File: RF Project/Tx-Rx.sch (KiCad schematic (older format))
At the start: 25 parts, among them U1 CC2500RGPR, U2 U.FL_male

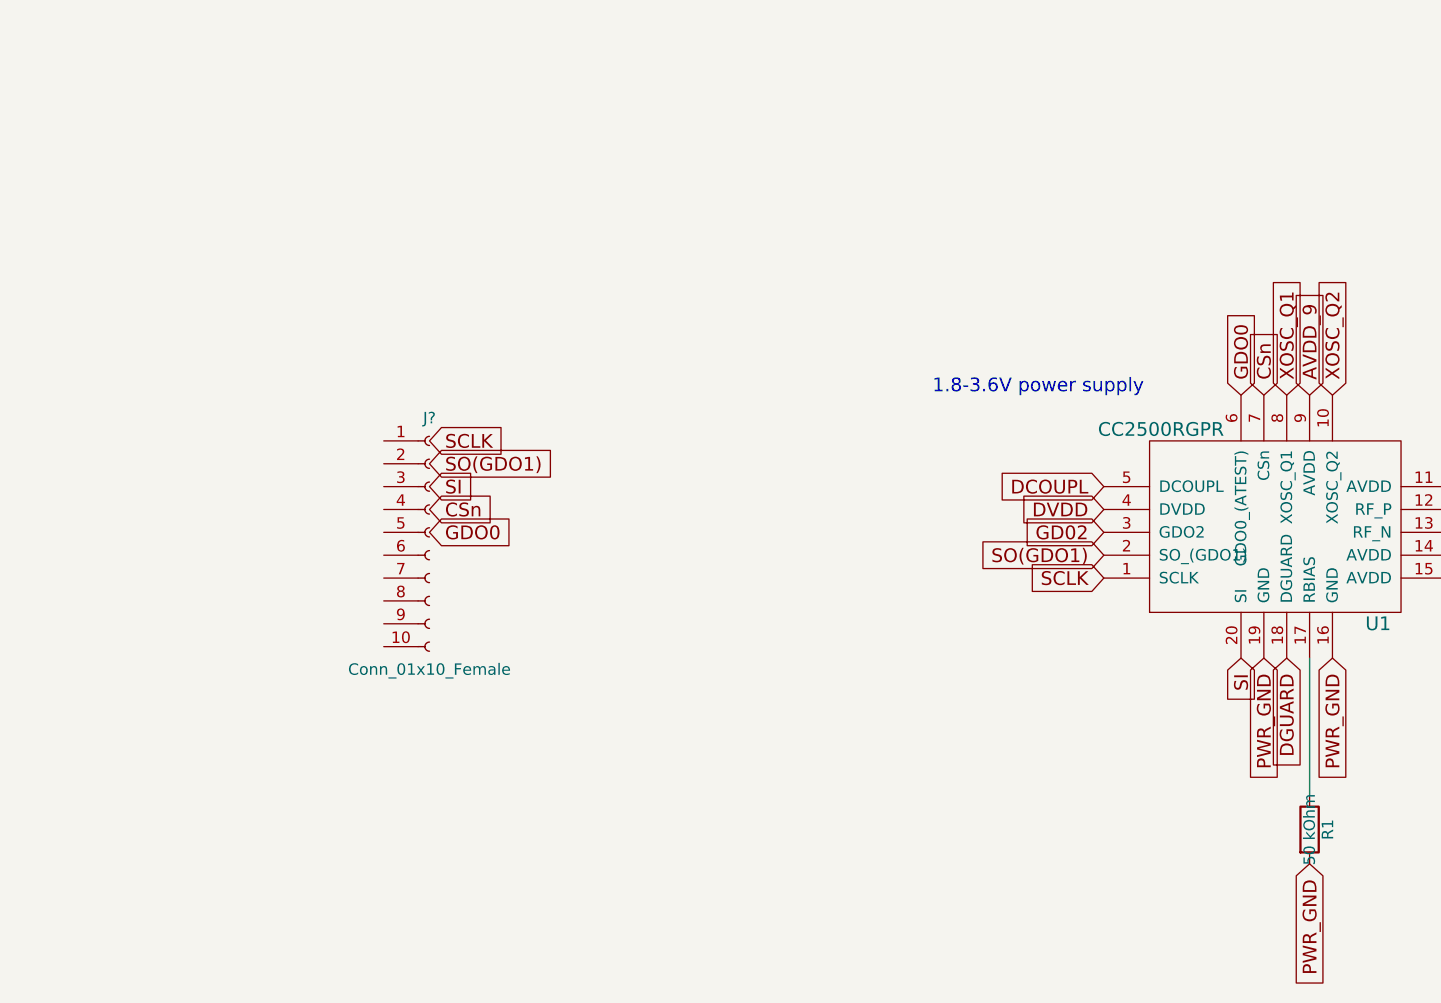
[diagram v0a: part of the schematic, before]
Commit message: Added Avionics Headers to schematic, fixed library link issues (hopefully) and started working on Layout
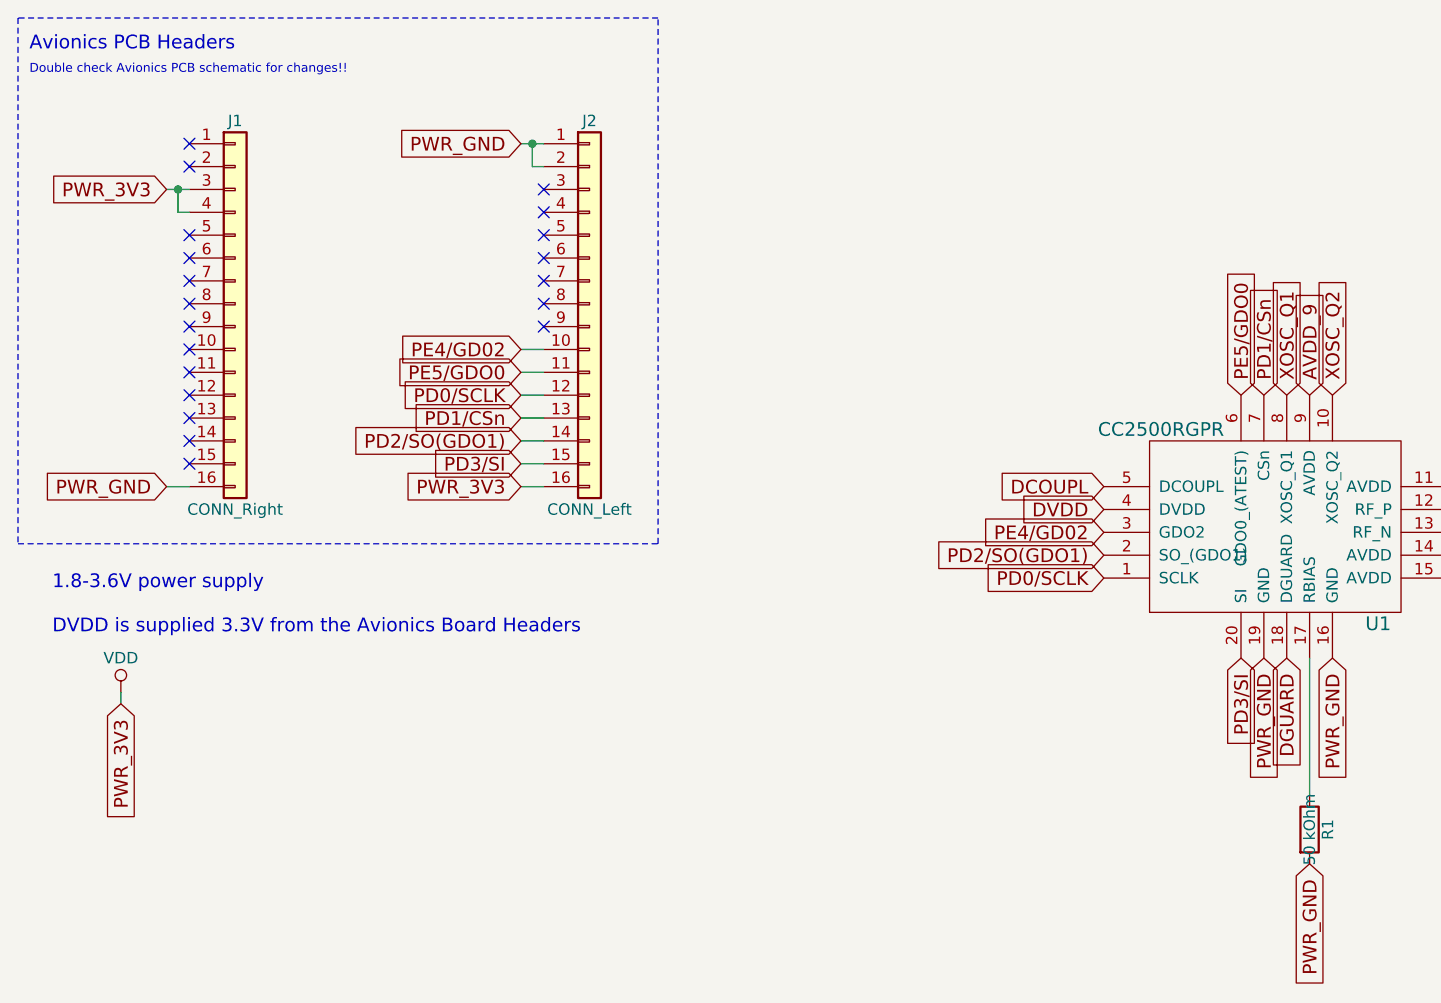
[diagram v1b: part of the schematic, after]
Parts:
- removed J?: Conn_01x10_Female, symbol Conn_01x10_Female
- added J1: CONN_Right, Pin_Headers:Pin_Header_Straight_1x16_Pitch2.54mm, symbol Conn_01x16
- added J2: CONN_Left, Pin_Headers:Pin_Header_Straight_1x16_Pitch2.54mm, symbol Conn_01x16
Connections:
- net GNDREF: now also J1.16 (Pin_16), J2.1 (Pin_1), J2.2 (Pin_2)
- net VDD: now also J1.3 (Pin_3), J1.4 (Pin_4), J2.16 (Pin_16)
- net CSn renamed PD1/CSn
- net PD1/CSn: now also J2.13 (Pin_13)
- net GD02 renamed PE4/GD02
- net PE4/GD02: now also J2.10 (Pin_10)
- net GDO0 renamed PE5/GDO0
- net PE5/GDO0: now also J2.11 (Pin_11)
- net SCLK renamed PD0/SCLK
- net PD0/SCLK: now also J2.12 (Pin_12)
- net SI renamed PD3/SI
- net PD3/SI: now also J2.15 (Pin_15)
- net SO(GDO1) renamed PD2/SO(GDO1)
- net PD2/SO(GDO1): now also J2.14 (Pin_14)
- no-connect marks 0 -> 20
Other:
- note added: "1.8-3.6V power supply\n\nDVDD is supplied 3.3V from the Avionics Board Headers\n"
- note added: "Avionics PCB Headers"
- note added: "Double check Avionics PCB schematic for changes!!"
- note removed: "1.8-3.6V power supply\n"

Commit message: Add files via upload
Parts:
- C14, C16, C17: value 220μF -> 220pF
- R1: footprint Resistors_SMD:R_0201 -> Resistors_SMD:R_0402
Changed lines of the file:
@@
 F 0 "R1" V 6330 4150 50  0000 C CNN
 F 1 "50 kOhm" V 6250 4150 50  0000 C CNN
-F 2 "Resistors_SMD:R_0201" V 6180 4150 50  0001 C CNN
+F 2 "Resistors_SMD:R_0402" V 6180 4150 50  0001 C CNN
 F 3 "" H 6250 4150 50  0001 C CNN
 	1    6250 4150
@@
 P 9550 1750
 F 0 "C14" H 9575 1850 50  0000 L CNN
-F 1 "220μF" H 9575 1650 50  0000 L CNN
+F 1 "220pF" H 9575 1650 50  0000 L CNN
 F 2 "Capacitors_SMD:C_0402" H 9588 1600 50  0001 C CNN
 F 3 "" H 9550 1750 50  0001 C CNN
@@
 P 10300 1750
 F 0 "C16" H 10325 1850 50  0000 L CNN
-F 1 "220μF" H 10325 1650 50  0000 L CNN
+F 1 "220pF" H 10325 1650 50  0000 L CNN
 F 2 "Capacitors_SMD:C_0402" H 10338 1600 50  0001 C CNN
 F 3 "" H 10300 1750 50  0001 C CNN
@@
 P 10550 2650
 F 0 "C17" H 10575 2750 50  0000 L CNN
-F 1 "220μF" H 10575 2550 50  0000 L CNN
+F 1 "220pF" H 10575 2550 50  0000 L CNN
 F 2 "Capacitors_SMD:C_0402" H 10588 2500 50  0001 C CNN
 F 3 "" H 10550 2650 50  0001 C CNN

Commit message: hello
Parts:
- R1: value 50 kOhm -> 56.2 kOhm; Digikey Part No. (none) -> CR0402-FX-5622GLFCT-ND
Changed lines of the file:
@@
 P 6250 4150
 F 0 "R1" V 6330 4150 50  0000 C CNN
-F 1 "50 kOhm" V 6250 4150 50  0000 C CNN
+F 1 "56.2 kOhm" V 6250 4150 50  0000 C CNN
 F 2 "Resistors_SMD:R_0402" V 6180 4150 50  0001 C CNN
 F 3 "" H 6250 4150 50  0001 C CNN
+F 4 "CR0402-FX-5622GLFCT-ND" V 6250 4150 60  0001 C CNN "Digikey Part No."
 	1    6250 4150
 	1    0    0    -1

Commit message: GPS schematic and pcb track routing
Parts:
- 26Mhtz1: footprint Crystals:Crystal_SMD_Abracon_ABM3B-4pin_5.0x3.2mm -> transciever_chip:CC2500
- C1: footprint Capacitors_SMD:C_0402 -> RF_Transciever:VENUS634FLPX
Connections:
- net RX: now reaches J1.8 (Pin_8)
- net TX: now reaches J1.9 (Pin_9)
- no-connect marks 20 -> 18
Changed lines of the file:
@@
 LIBS:cc2500rgpr
 LIBS:Tx-Rx-cache
+LIBS:rocketGPS
 EELAYER 25 0
 EELAYER END
 $Descr A4 11693 8268
 encoding utf-8
-Sheet 1 1
+Sheet 1 2
 Title "Model Rocket Transciever Design"
 Date "2018-07-13"
@@
 F 0 "26Mhtz1" H 8200 4250 50  0000 C CNN
 F 1 "Crystal" H 8200 3950 50  0000 C CNN
-F 2 "Crystals:Crystal_SMD_Abracon_ABM3B-4pin_5.0x3.2mm" H 8200 4100 50  0001 C CNN
+F 2 "transciever_chip:CC2500" H 8200 4100 50  0001 C CNN
 F 3 "" H 8200 4100 50  0001 C CNN
 	1    8200 4100
@@
 F 0 "C1" H 8125 5500 50  0000 L CNN
 F 1 "100pF" H 8125 5300 50  0000 L CNN
-F 2 "Capacitors_SMD:C_0402" H 8138 5250 50  0001 C CNN
+F 2 "RF_Transciever:VENUS634FLPX" H 8138 5250 50  0001 C CNN
 F 3 "" H 8100 5400 50  0001 C CNN
 	1    8100 5400
@@
 NoConn ~ 1350 1250
 NoConn ~ 1350 1550
-NoConn ~ 1350 1650
 NoConn ~ 1350 1750
-NoConn ~ 1350 1850
-NoConn ~ 1350 1950
-NoConn ~ 1350 2050
 NoConn ~ 1350 2150
 Wire Wire Line
@@
 Wire Wire Line
 	1050 3600 1050 3550
+$Sheet
+S 1350 4300 1475 800
+U 5B569403
+F0 "GPS" 60
+F1 "GPS.sch" 60
+F2 "3V3" I L 1350 4500 60
+F3 "PWR_GND" I L 1350 4825 60
+F4 "TX" I R 2825 4475 60
+F5 "RX" I R 2825 4600 60
+$EndSheet
+Text GLabel 1300 4825 0    60   Input ~ 0
+PWR_GND
+Text GLabel 1300 4500 0    60   Input ~ 0
+PWR_3V3
+Wire Wire Line
+	1300 4500 1350 4500
+Wire Wire Line
+	1300 4825 1350 4825
+NoConn ~ 1350 1650
+Text GLabel 2925 4475 2    60   Input ~ 0
+TX
+Text GLabel 2925 4600 2    60   Input ~ 0
+RX
+Wire Wire Line
+	2925 4600 2825 4600
+Wire Wire Line
+	2825 4475 2925 4475
+Text GLabel 1250 1850 0    60   Input ~ 0
+RX
+Text GLabel 1250 1950 0    60   Input ~ 0
+TX
+Wire Wire Line
+	1350 1850 1250 1850
+Wire Wire Line
+	1250 1950 1350 1950
+NoConn ~ 1350 2050
 $EndSCHEMATC
